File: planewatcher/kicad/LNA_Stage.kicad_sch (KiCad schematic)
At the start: 8 parts, among them U7 TQP3M9036

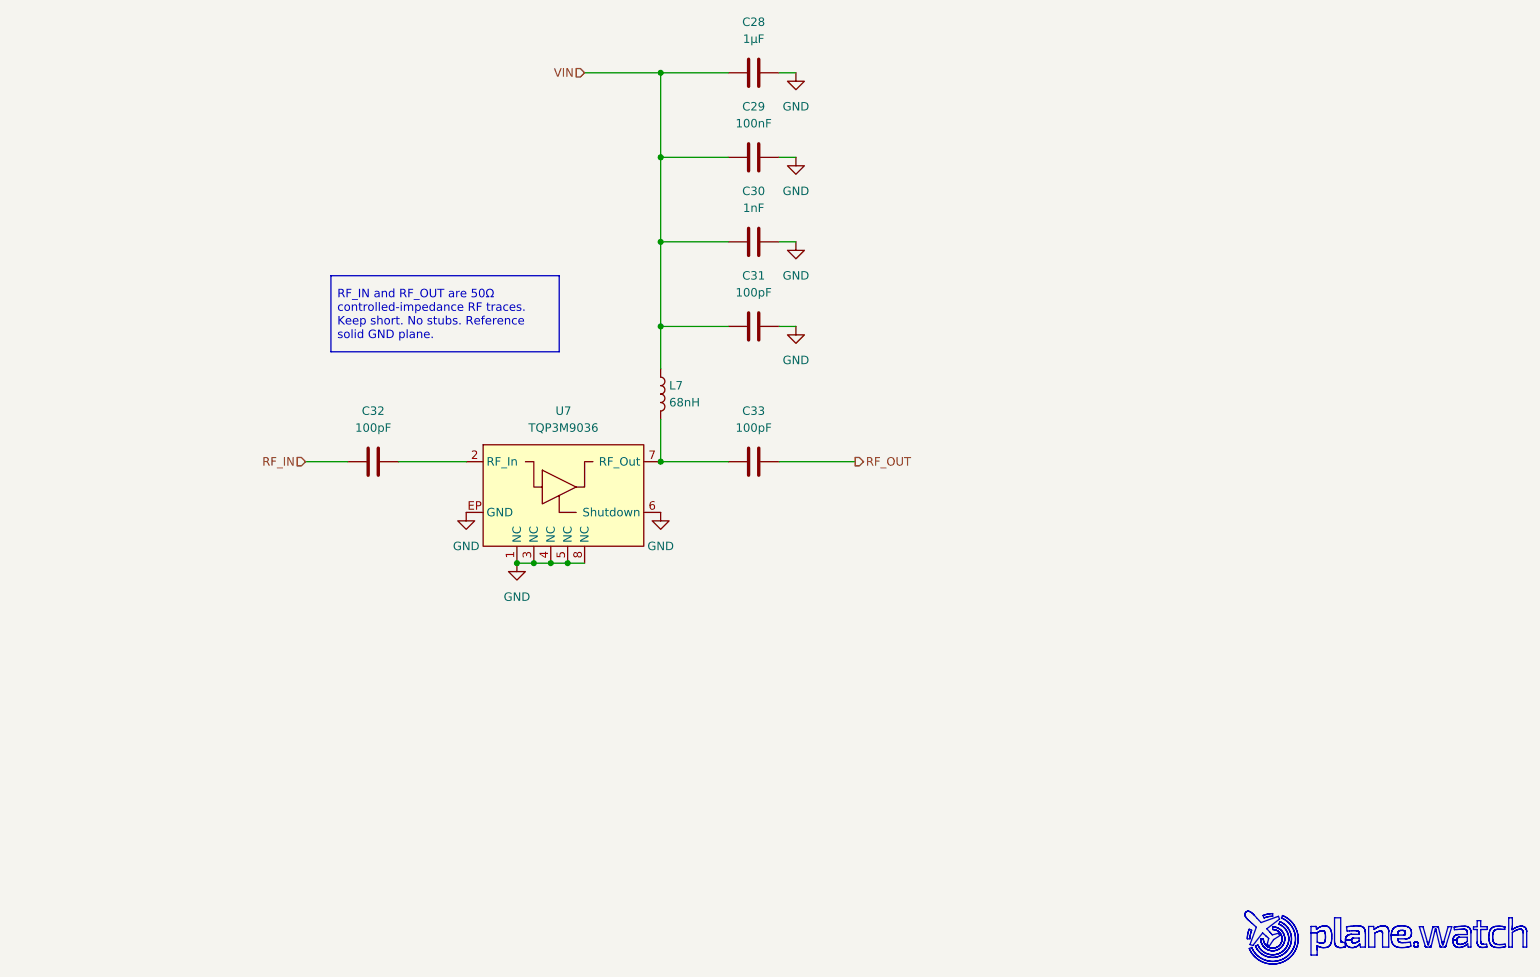
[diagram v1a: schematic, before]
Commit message: Add RF pi matching networks + more
- Remove EEPROM write project solder jumper
- Update proto 1.3 documentation
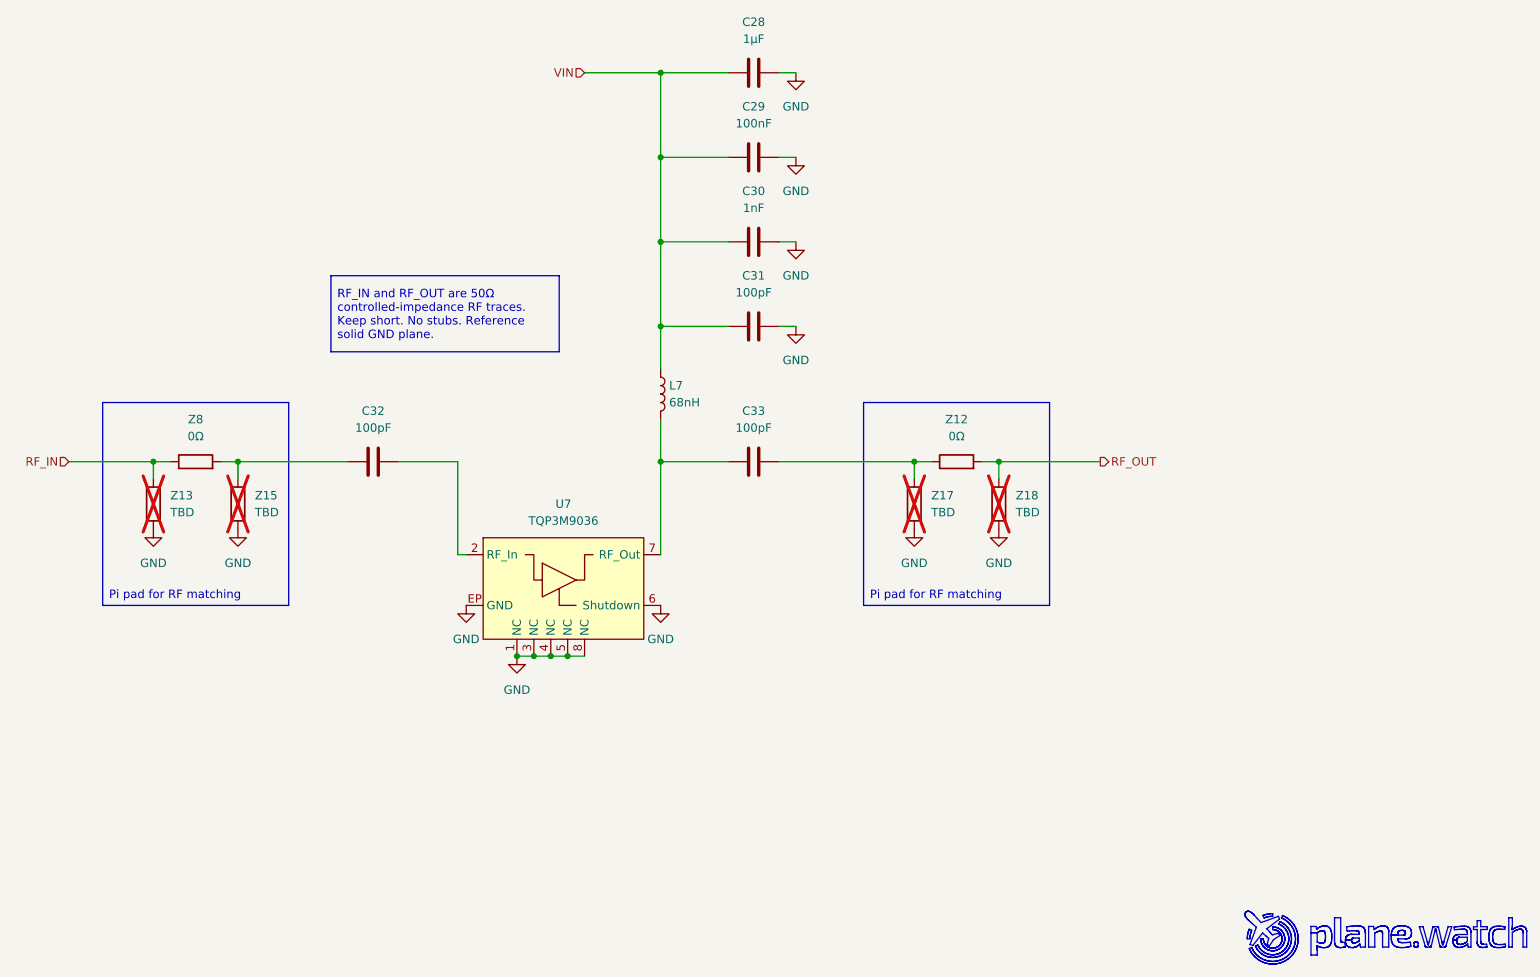
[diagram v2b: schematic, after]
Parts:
- added Z12, Z8: 0Ω, Resistor_SMD:R_0402_1005Metric, symbol Device:R
- added Z13, Z15, Z17, Z18: TBD, Resistor_SMD:R_0402_1005Metric, symbol Device:R
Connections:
- net GND: now also Z13.1, Z15.1, Z17.1, Z18.1
- net RF_IN: now also Z13.2, Z8.1; no longer C32.2
- net RF_OUT: now also Z12.2, Z18.2; no longer C33.1
- new net: C33.1, Z12.1, Z17.2
- new net: C32.2, Z15.2, Z8.2
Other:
- moved on the sheet: U7

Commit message: Change LCSC column name, add fabrication toolkit options
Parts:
- C28: LCSC (none) -> C528974; lcsc_id C528974 -> (none)
- C29: LCSC (none) -> C161163; lcsc_id C161163 -> (none)
- C30: LCSC (none) -> C126493; lcsc_id C126493 -> (none)
- C31, C32, C33: LCSC (none) -> C2941926; lcsc_id C2941926 -> (none)
- L7: LCSC (none) -> C19191685; lcsc_id C19191685 -> (none)
- U7: LCSC (none) -> C920261; lcsc_id C920261 -> (none)
- Z12, Z8: LCSC (none) -> C242160; lcsc_id C242160 -> (none)
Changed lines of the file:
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@@
 			(justify left bottom)
 		)
-		(property "Netclass" "RF_50Ω"
+		(property "Net Class" "RF_50Ω"
 			(at 120.0785 99.06 0)
 			(show_name no)
@@
 			)
 		)
-		(property "lcsc_id" "C528974"
+		(property "LCSC" "C528974"
 			(at 167.64 45.72 0)
 			(hide yes)
@@
 			)
 		)
-		(property "lcsc_id" "C2941926"
+		(property "LCSC" "C2941926"
 			(at 110.49 104.14 0)
 			(hide yes)
@@
 			)
 		)
-		(property "lcsc_id" "C2941926"
+		(property "LCSC" "C2941926"
 			(at 167.64 104.14 0)
 			(hide yes)
@@
 			)
 		)
-		(property "lcsc_id" "C242160"
+		(property "LCSC" "C242160"
 			(at 198.12 104.14 90)
 			(hide yes)
@@
 			)
 		)
-		(property "lcsc_id" "C242160"
+		(property "LCSC" "C242160"
 			(at 83.82 104.14 90)
 			(hide yes)
@@
 			)
 		)
-		(property "lcsc_id" "C161163"
+		(property "LCSC" "C161163"
 			(at 167.64 58.42 0)
 			(hide yes)
@@
 			)
 		)
-		(property "lcsc_id" "C126493"
+		(property "LCSC" "C126493"
 			(at 167.64 71.12 0)
 			(hide yes)
@@
 			)
 		)
-		(property "lcsc_id" "C920261"
+		(property "LCSC" "C920261"
 			(at 138.43 114.3 0)
 			(hide yes)
@@
 			)
 		)
-		(property "lcsc_id" "C2941926"
+		(property "LCSC" "C2941926"
 			(at 167.64 83.82 0)
 			(hide yes)
@@
 			)
 		)
-		(property "lcsc_id" "C19191685"
+		(property "LCSC" "C19191685"
 			(at 153.67 93.98 0)
 			(hide yes)

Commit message: Adjust component grouping
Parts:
- C29: value 100nF -> 0.1µF
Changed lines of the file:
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@@
 			)
 		)
-		(property "Value" "100nF"
+		(property "Value" "0.1µF"
 			(at 167.64 53.34 90)
 			(show_name no)

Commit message: Populate Z13 with 68nH
After initial testing of the prototype 1.3, Z13 was populated with 68nH which improved RF performance significantly.
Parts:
- Z13: value TBD -> 68nH; footprint Resistor_SMD:R_0402_1005Metric -> Inductor_SMD:L_0402_1005Metric; LCSC (none) -> C3221883; MPN (none) -> 0402DC-68NXJRW; Manufacturer (none) -> Coilcraft
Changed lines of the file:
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@@
 	(title_block
 		(title "Plane Watcher")
-		(date "2026-07-19")
-		(rev "prototype 1.3")
+		(date "2026-09-25")
+		(rev "1.4")
 		(company "plane.watch")
 		(comment 1 "No warranty; see LICENSE.")
@@
 					(reference "Z17")
 					(unit 1)
+					(variant
+						(name "revision_1.4")
+					)
 				)
 				(path "/7a4a4324-e8b8-4d06-b75a-28095d4e9f10/ddba7db9-116b-4903-8726-853149ab65d1"
 					(reference "Z19")
 					(unit 1)
+					(variant
+						(name "revision_1.4")
+					)
 				)
 			)
@@
 					(reference "C28")
 					(unit 1)
+					(variant
+						(name "revision_1.4")
+					)
 				)
 				(path "/7a4a4324-e8b8-4d06-b75a-28095d4e9f10/ddba7db9-116b-4903-8726-853149ab65d1"
 					(reference "C34")
 					(unit 1)
+					(variant
+						(name "revision_1.4")
+					)
 				)
 			)
@@
 					(reference "C32")
 					(unit 1)
+					(variant
+						(name "revision_1.4")
+					)
 				)
 				(path "/7a4a4324-e8b8-4d06-b75a-28095d4e9f10/ddba7db9-116b-4903-8726-853149ab65d1"
 					(reference "C38")
 					(unit 1)
+					(variant
+						(name "revision_1.4")
+					)
 				)
 			)
@@
 					(reference "C33")
 					(unit 1)
+					(variant
+						(name "revision_1.4")
+					)
 				)
 				(path "/7a4a4324-e8b8-4d06-b75a-28095d4e9f10/ddba7db9-116b-4903-8726-853149ab65d1"
 					(reference "C39")
 					(unit 1)
+					(variant
+						(name "revision_1.4")
+					)
 				)
 			)
@@
 					(reference "Z12")
 					(unit 1)
+					(variant
+						(name "revision_1.4")
+					)
 				)
 				(path "/7a4a4324-e8b8-4d06-b75a-28095d4e9f10/ddba7db9-116b-4903-8726-853149ab65d1"
 					(reference "Z20")
 					(unit 1)
+					(variant
+						(name "revision_1.4")
+					)
 				)
 			)
@@
 					(reference "Z8")
 					(unit 1)
+					(variant
+						(name "revision_1.4")
+					)
 				)
 				(path "/7a4a4324-e8b8-4d06-b75a-28095d4e9f10/ddba7db9-116b-4903-8726-853149ab65d1"
 					(reference "R9")
 					(unit 1)
+					(variant
+						(name "revision_1.4")
+					)
 				)
 			)
@@
 					(reference "C29")
 					(unit 1)
+					(variant
+						(name "revision_1.4")
+					)
 				)
 				(path "/7a4a4324-e8b8-4d06-b75a-28095d4e9f10/ddba7db9-116b-4903-8726-853149ab65d1"
 					(reference "C35")
 					(unit 1)
+					(variant
+						(name "revision_1.4")
+					)
 				)
 			)
@@
 			)
 		)
-		(property "Value" "TBD"
+		(property "Value" "68nH"
 			(at 80.01 111.7599 0)
 			(show_name no)
@@
 			)
 		)
-		(property "Footprint" "Resistor_SMD:R_0402_1005Metric"
+		(property "Footprint" "Inductor_SMD:L_0402_1005Metric"
 			(at 79.248 110.49 90)
 			(hide yes)
@@
 			)
 		)
-		(property "Description" "First shunt element in pi pad"
+		(property "Description" "First shunt element in pi pad, populated after initial testing of proto 1.3"
 			(at 77.47 110.49 0)
 			(hide yes)
@@
 			)
 		)
+		(property "LCSC" "C3221883"
+			(at 77.47 110.49 0)
+			(hide yes)
+			(show_name no)
+			(do_not_autoplace no)
+			(effects
+				(font
+					(size 1.27 1.27)
+				)
+			)
+		)
+		(property "MPN" "0402DC-68NXJRW"
+			(at 77.47 110.49 0)
+			(hide yes)
+			(show_name no)
+			(do_not_autoplace no)
+			(effects
+				(font
+					(size 1.27 1.27)
+				)
+			)
+		)
+		(property "Manufacturer" "Coilcraft"
+			(at 77.47 110.49 0)
+			(hide yes)
+			(show_name no)
+			(do_not_autoplace no)
+			(effects
+				(font
+					(size 1.27 1.27)
+				)
+			)
+		)
 		(pin "2"
 		)
@@
 					(reference "Z13")
 					(unit 1)
+					(variant
+						(name "revision_1.4")
+						(dnp no)
+						(in_bom yes)
+					)
 				)
 				(path "/7a4a4324-e8b8-4d06-b75a-28095d4e9f10/ddba7db9-116b-4903-8726-853149ab65d1"
 					(reference "Z14")
 					(unit 1)
+					(variant
+						(name "revision_1.4")
+					)
 				)
 			)
@@
 					(reference "C30")
 					(unit 1)
+					(variant
+						(name "revision_1.4")
+					)
 				)
 				(path "/7a4a4324-e8b8-4d06-b75a-28095d4e9f10/ddba7db9-116b-4903-8726-853149ab65d1"
 					(reference "C36")
 					(unit 1)
+					(variant
+						(name "revision_1.4")
+					)
 				)
 			)
@@
 					(reference "Z18")
 					(unit 1)
+					(variant
+						(name "revision_1.4")
+					)
 				)
 				(path "/7a4a4324-e8b8-4d06-b75a-28095d4e9f10/ddba7db9-116b-4903-8726-853149ab65d1"
 					(reference "Z21")
 					(unit 1)
+					(variant
+						(name "revision_1.4")
+					)
 				)
 			)
@@
 					(reference "U7")
 					(unit 1)
+					(variant
+						(name "revision_1.4")
+					)
 				)
 				(path "/7a4a4324-e8b8-4d06-b75a-28095d4e9f10/ddba7db9-116b-4903-8726-853149ab65d1"
 					(reference "U8")
 					(unit 1)
+					(variant
+						(name "revision_1.4")
+					)
 				)
 			)
@@
 					(reference "Z15")
 					(unit 1)
+					(variant
+						(name "revision_1.4")
+					)
 				)
 				(path "/7a4a4324-e8b8-4d06-b75a-28095d4e9f10/ddba7db9-116b-4903-8726-853149ab65d1"
 					(reference "Z16")
 					(unit 1)
+					(variant
+						(name "revision_1.4")
+					)
 				)
 			)
@@
 					(reference "C31")
 					(unit 1)
+					(variant
+						(name "revision_1.4")
+					)
 				)
 				(path "/7a4a4324-e8b8-4d06-b75a-28095d4e9f10/ddba7db9-116b-4903-8726-853149ab65d1"
 					(reference "C37")
 					(unit 1)
+					(variant
+						(name "revision_1.4")
+					)
 				)
 			)
@@
 					(reference "L7")
 					(unit 1)
+					(variant
+						(name "revision_1.4")
+					)
 				)
 				(path "/7a4a4324-e8b8-4d06-b75a-28095d4e9f10/ddba7db9-116b-4903-8726-853149ab65d1"
 					(reference "L8")
 					(unit 1)
+					(variant
+						(name "revision_1.4")
+					)
 				)
 			)
